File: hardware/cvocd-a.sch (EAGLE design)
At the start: 71 parts, among them IC1 PIC16F1825SO14, IC2 74HC595D, IC3 74HC595D, IC4 MCP4728_QUAD_DAC, IC5 LM324D, IC6 REG1117, IC7 6N138

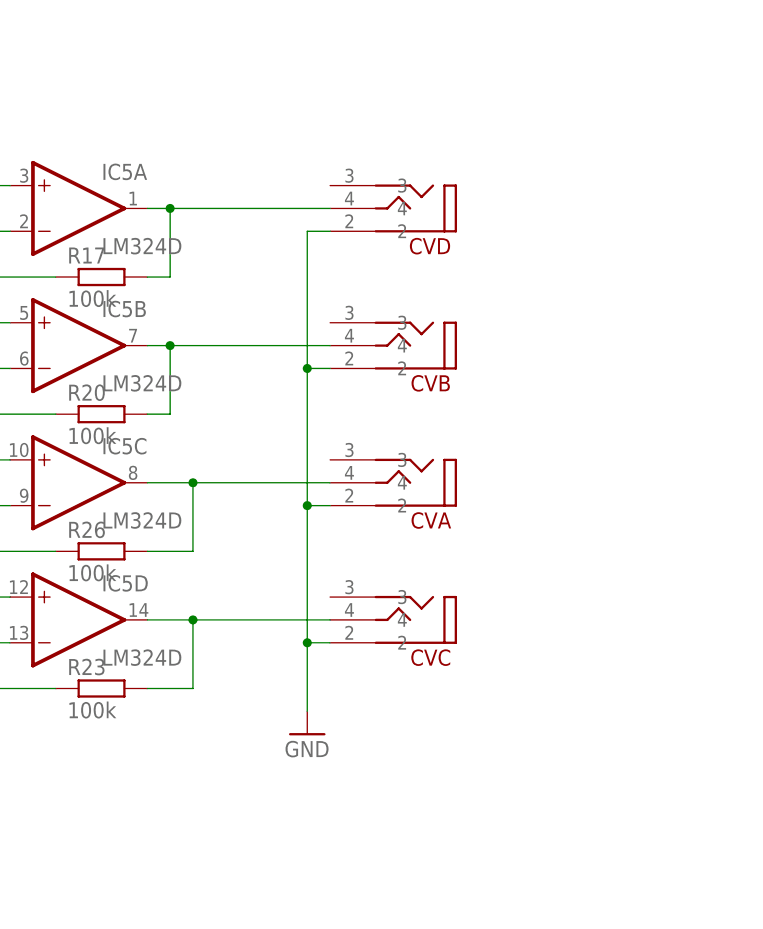
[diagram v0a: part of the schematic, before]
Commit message: icsp to top layer, current lim resistors
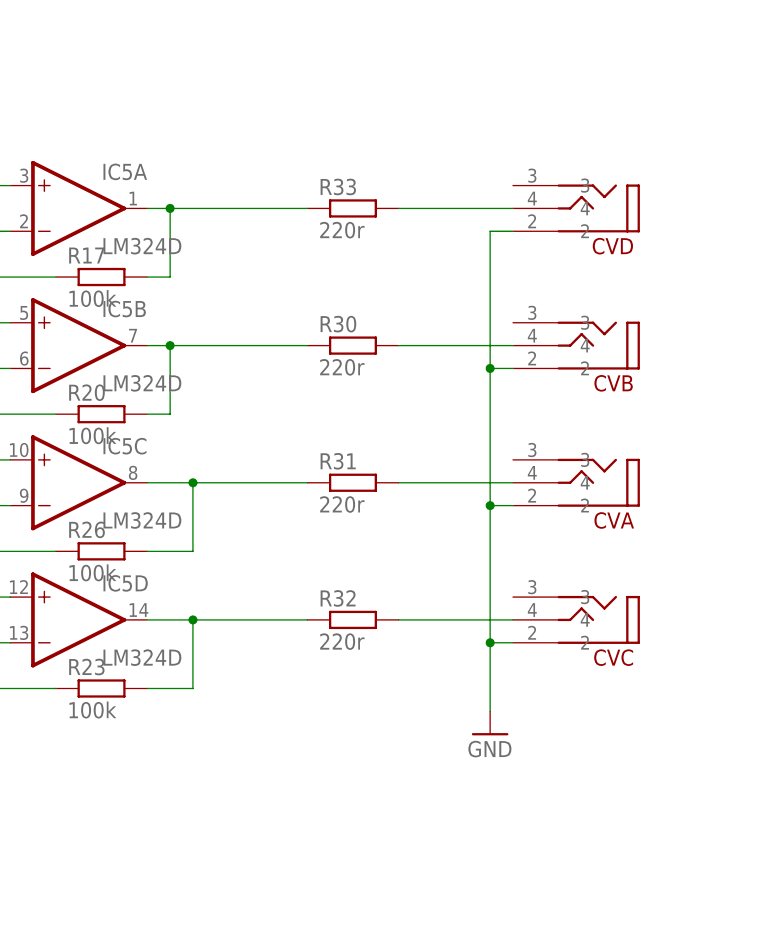
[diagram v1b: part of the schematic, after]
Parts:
- added R30, R31, R32, R33: 220r, rcl:R-EU_R0805
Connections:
- new net N$10: CVD.4, R33.2
- new net N$11: CVB.4, R30.2
- new net N$14: CVA.4, R31.2
- new net N$17: CVC.4, R32.2
- net N$2: now also R33.1; no longer CVD.4
- net N$3: now also R30.1; no longer CVB.4
- net N$4: now also R31.1; no longer CVA.4
- net N$5: now also R32.1; no longer CVC.4
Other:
- moved on the sheet: CVA, CVB, CVC, CVD
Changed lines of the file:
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@@
 <part name="C20" library="rcl" deviceset="CPOL-EU" device="C"/>
 <part name="D2" library="diode" deviceset="DIODE-" device="SOD123"/>
+<part name="R33" library="rcl" deviceset="R-EU_" device="R0805" value="220r"/>
+<part name="R30" library="rcl" deviceset="R-EU_" device="R0805" value="220r"/>
+<part name="R31" library="rcl" deviceset="R-EU_" device="R0805" value="220r"/>
+<part name="R32" library="rcl" deviceset="R-EU_" device="R0805" value="220r"/>
 </parts>
 <sheets>
@@
 </plain>
 <instances>
-<instance part="CVB" gate="G$1" x="152.4" y="99.06" rot="R180"/>
-<instance part="CVD" gate="G$1" x="152.4" y="114.3" rot="R180"/>
-<instance part="CVA" gate="G$1" x="152.4" y="83.82" rot="R180"/>
-<instance part="CVC" gate="G$1" x="152.4" y="68.58" rot="R180"/>
+<instance part="CVB" gate="G$1" x="172.72" y="99.06" rot="R180"/>
+<instance part="CVD" gate="G$1" x="172.72" y="114.3" rot="R180"/>
+<instance part="CVA" gate="G$1" x="172.72" y="83.82" rot="R180"/>
+<instance part="CVC" gate="G$1" x="172.72" y="68.58" rot="R180"/>
 <instance part="GATE4" gate="G$1" x="-15.24" y="17.78" smashed="yes" rot="R180">
 <attribute name="NAME" x="-1.778" y="17.018" size="1.778" layer="94" rot="R180"/>
@@
 <instance part="R24" gate="G$1" x="96.52" y="60.96"/>
 <instance part="GND1" gate="1" x="88.9" y="55.88"/>
-<instance part="GND13" gate="1" x="139.7" y="55.88"/>
+<instance part="GND13" gate="1" x="160.02" y="55.88"/>
 <instance part="IC3" gate="P" x="-134.62" y="-17.78" rot="R270"/>
 <instance part="GND14" gate="1" x="-149.86" y="-30.48"/>
@@
 <instance part="C20" gate="G$1" x="-55.88" y="167.64"/>
 <instance part="D2" gate="G$1" x="-106.68" y="175.26"/>
+<instance part="R33" gate="G$1" x="144.78" y="114.3"/>
+<instance part="R30" gate="G$1" x="144.78" y="99.06"/>
+<instance part="R31" gate="G$1" x="144.78" y="83.82"/>
+<instance part="R32" gate="G$1" x="144.78" y="68.58"/>
 </instances>
 <busses>
@@
 </segment>
 <segment>
-<wire x1="139.7" y1="111.76" x2="139.7" y2="96.52" width="0.1524" layer="91"/>
-<wire x1="139.7" y1="96.52" x2="139.7" y2="81.28" width="0.1524" layer="91"/>
-<wire x1="139.7" y1="81.28" x2="139.7" y2="66.04" width="0.1524" layer="91"/>
-<wire x1="139.7" y1="66.04" x2="139.7" y2="58.42" width="0.1524" layer="91"/>
+<wire x1="160.02" y1="111.76" x2="160.02" y2="96.52" width="0.1524" layer="91"/>
+<wire x1="160.02" y1="96.52" x2="160.02" y2="81.28" width="0.1524" layer="91"/>
+<wire x1="160.02" y1="81.28" x2="160.02" y2="66.04" width="0.1524" layer="91"/>
+<wire x1="160.02" y1="66.04" x2="160.02" y2="58.42" width="0.1524" layer="91"/>
 <pinref part="CVA" gate="G$1" pin="2"/>
-<wire x1="142.24" y1="81.28" x2="139.7" y2="81.28" width="0.1524" layer="91"/>
-<junction x="139.7" y="81.28"/>
+<wire x1="162.56" y1="81.28" x2="160.02" y2="81.28" width="0.1524" layer="91"/>
+<junction x="160.02" y="81.28"/>
 <pinref part="CVC" gate="G$1" pin="2"/>
-<wire x1="142.24" y1="66.04" x2="139.7" y2="66.04" width="0.1524" layer="91"/>
-<junction x="139.7" y="66.04"/>
+<wire x1="162.56" y1="66.04" x2="160.02" y2="66.04" width="0.1524" layer="91"/>
+<junction x="160.02" y="66.04"/>
 <pinref part="GND13" gate="1" pin="GND"/>
 <pinref part="CVD" gate="G$1" pin="2"/>
-<wire x1="139.7" y1="111.76" x2="142.24" y2="111.76" width="0.1524" layer="91"/>
+<wire x1="160.02" y1="111.76" x2="162.56" y2="111.76" width="0.1524" layer="91"/>
 <pinref part="CVB" gate="G$1" pin="2"/>
-<wire x1="142.24" y1="96.52" x2="139.7" y2="96.52" width="0.1524" layer="91"/>
-<junction x="139.7" y="96.52"/>
+<wire x1="162.56" y1="96.52" x2="160.02" y2="96.52" width="0.1524" layer="91"/>
+<junction x="160.02" y="96.52"/>
 </segment>
 <segment>
@@
 <wire x1="124.46" y1="106.68" x2="124.46" y2="114.3" width="0.1524" layer="91"/>
 <junction x="124.46" y="114.3"/>
-<pinref part="CVD" gate="G$1" pin="4"/>
-<wire x1="124.46" y1="114.3" x2="142.24" y2="114.3" width="0.1524" layer="91"/>
+<wire x1="124.46" y1="114.3" x2="139.7" y2="114.3" width="0.1524" layer="91"/>
+<pinref part="R33" gate="G$1" pin="1"/>
 </segment>
 </net>
@@
 <wire x1="124.46" y1="91.44" x2="124.46" y2="99.06" width="0.1524" layer="91"/>
 <junction x="124.46" y="99.06"/>
-<pinref part="CVB" gate="G$1" pin="4"/>
-<wire x1="124.46" y1="99.06" x2="142.24" y2="99.06" width="0.1524" layer="91"/>
+<wire x1="124.46" y1="99.06" x2="139.7" y2="99.06" width="0.1524" layer="91"/>
+<pinref part="R30" gate="G$1" pin="1"/>
 </segment>
 </net>
@@
 <wire x1="121.92" y1="76.2" x2="127" y2="76.2" width="0.1524" layer="91"/>
 <wire x1="127" y1="76.2" x2="127" y2="83.82" width="0.1524" layer="91"/>
-<pinref part="CVA" gate="G$1" pin="4"/>
-<wire x1="127" y1="83.82" x2="142.24" y2="83.82" width="0.1524" layer="91"/>
+<wire x1="127" y1="83.82" x2="139.7" y2="83.82" width="0.1524" layer="91"/>
 <junction x="127" y="83.82"/>
+<pinref part="R31" gate="G$1" pin="1"/>
 </segment>
 </net>
@@
 <wire x1="121.92" y1="60.96" x2="127" y2="60.96" width="0.1524" layer="91"/>
 <wire x1="127" y1="60.96" x2="127" y2="68.58" width="0.1524" layer="91"/>
-<pinref part="CVC" gate="G$1" pin="4"/>
-<wire x1="127" y1="68.58" x2="142.24" y2="68.58" width="0.1524" layer="91"/>
+<wire x1="127" y1="68.58" x2="139.7" y2="68.58" width="0.1524" layer="91"/>
 <junction x="127" y="68.58"/>
+<pinref part="R32" gate="G$1" pin="1"/>
 </segment>
 </net>
@@
 </segment>
 </net>
+<net name="N$10" class="0">
+<segment>
+<pinref part="R33" gate="G$1" pin="2"/>
+<pinref part="CVD" gate="G$1" pin="4"/>
+<wire x1="149.86" y1="114.3" x2="162.56" y2="114.3" width="0.1524" layer="91"/>
+</segment>
+</net>
+<net name="N$11" class="0">
+<segment>
+<pinref part="R30" gate="G$1" pin="2"/>
+<pinref part="CVB" gate="G$1" pin="4"/>
+<wire x1="149.86" y1="99.06" x2="162.56" y2="99.06" width="0.1524" layer="91"/>
+</segment>
+</net>
+<net name="N$14" class="0">
+<segment>
+<pinref part="R31" gate="G$1" pin="2"/>
+<pinref part="CVA" gate="G$1" pin="4"/>
+<wire x1="149.86" y1="83.82" x2="162.56" y2="83.82" width="0.1524" layer="91"/>
+</segment>
+</net>
+<net name="N$17" class="0">
+<segment>
+<pinref part="R32" gate="G$1" pin="2"/>
+<pinref part="CVC" gate="G$1" pin="4"/>
+<wire x1="149.86" y1="68.58" x2="162.56" y2="68.58" width="0.1524" layer="91"/>
+</segment>
+</net>

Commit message: working on v4
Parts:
- removed C18: 100n, rcl:C-EUC0805
- added PA, PB, PC, PD: (no value), rcl:R-TRIMM3314G
- IC1: value PIC16F1825SO14 -> 6N138; device jasons_stuff:PIC16F1825SO14 -> optocoupler:6N138
- IC2: value 74HC595D -> LM324D; device 74xx-eu:74HC595D -> linear:LM324D
- IC3: value 74HC595D -> MCP4728_QUAD_DAC; device 74xx-eu:74HC595D -> jason_eagle6:MCP4728_QUAD_DAC
- IC4: value MCP4728_QUAD_DAC -> REG1117; device jason_eagle6:MCP4728_QUAD_DAC -> burr-brown:REG1117
- IC5: value LM324D -> PIC16F1825SO14; device linear:LM324D -> jasons_stuff:PIC16F1825SO14
- IC6: value REG1117 -> 74HC595D; device burr-brown:REG1117 -> 74xx-eu:74HC595D
- IC7: value 6N138 -> 74HC595D; device optocoupler:6N138 -> 74xx-eu:74HC595D
- R10, R11, R8, R9: value (none) -> 220r
- R12, R13, R14, R15, R5, R6, R7: value (none) -> 100k
- R17, R18, R19, R23, R24, R25, R26: value 100k -> (none)
- R2, R3: value (none) -> 1k5
- R20: value 100k -> 4k7
- R22: value 4k7 -> 10k
- R27, R28: value 1k5 -> (none)
- R30, R31, R32, R33: value 220r -> (none)
- R4: value 10k -> 100k
- renumbered C10 to C5, C11 to C6, C12 to C8, C13 to C7, C19 to C1, C20 to C2, C21 to C3, C9 to C4, L1 to LED1, L2 to LED2, L3 to LED3, S1 to SW1
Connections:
- new net N$18: CVD.4, R5.2, R8.2
- new net N$19: CVB.4, R7.2, R9.2
- new net N$38: CVA.4, R11.2, R14.2
- new net N$44: CVC.4, R10.2, R12.2
- new net N$45: PA.E, R15.2
- new net N$54: PA.A, R14.1
- new net N$55: PC.E, R13.2
- new net N$56: PC.A, R12.1
- net ACT_LED: now also IC5.RA2/INT; no longer IC1.RA2/INT
- net GND: now also IC1.GND, IC2P.V-, IC3.LDAC#, IC3.VSS, IC4.GND, IC5.VSS, IC6A.G, IC6P.GND, IC7A.G, IC7P.GND, R13.1, R15.1, R23.2, R24.2, R25.2, R4.1, R6.1; no longer C18.2, IC1.VSS, IC2A.G, IC2P.GND, IC3A.G, IC3P.GND, IC4.LDAC#, IC4.VSS, IC5P.V-, IC6.GND, IC7.GND, R1.2, R18.1, R19.1, R2.2, R24.1, R25.1, R28.2
- net MIDI_IN: now also IC1.VO, IC5.RC5/RX, R2.1; no longer IC1.RC5/RX, IC7.VO, R27.1
- net MIDI_OUT: now also IC5.RC4/TX; no longer IC1.RC4/TX
- net N$1: now also R19.2; no longer R15.2
- net N$10: now also IC2A.-IN, PD.S; no longer CVD.4, R33.2
- net N$11: now also IC2C.-IN, PA.S; no longer CVB.4, R30.2
- net N$12: now also IC6A.QA, R19.1; no longer IC3A.QA, R15.1
- net N$13: now also IC6A.QB, R18.1; no longer IC3A.QB, R16.1
- net N$14: now also IC2D.-IN, PC.S; no longer CVA.4, R31.2
- net N$15: now also IC6A.QD, R17.1; no longer IC3A.QD, R13.1
- net N$16: now also IC6A.QC, R16.1; no longer IC3A.QC, R14.1
- net N$17: now also PD.E, R4.2; no longer CVC.4, R32.2
- net N$2: now also IC2A.OUT, R8.1; no longer IC5A.OUT, R17.2, R33.1
- net N$20: now also R26.2; no longer R8.2
- net N$21: now also IC3.SCL, IC5.RCO/SCL/SCK, R21.2; no longer IC1.RCO/SCL/SCK, IC4.SCL, R22.2
- net N$22: now also IC3.SDA, IC5.RC1/SDA/SDI, R20.2; no longer IC1.RC1/SDA/SDI, IC4.SDA, R21.2
- net N$23: now also R27.2; no longer R7.2
- net N$24: now also R28.2; no longer R6.2
- net N$25: now also PD.A, R5.1; no longer IC5A.-IN, R17.1, R18.2
- net N$26: now also IC2B.-IN, PB.S; no longer IC5B.-IN, R19.2, R20.1
- net N$27: now also PB.E, R6.2; no longer IC5C.-IN, R25.2, R26.1
- net N$28: now also PB.A, R7.1; no longer IC5D.-IN, R23.1, R24.2
- net N$29: now also R1.1; no longer R29.1
- net N$3: now also IC2B.OUT, R9.1; no longer IC5B.OUT, R20.2, R30.1
- net N$30: now also IC1.A, R1.2; no longer IC7.A, R29.2
- net N$31: now also IC1.C; no longer IC7.C
- net N$32: now also R29.2; no longer R5.2
- net N$33: now also R30.2; no longer R12.2
- net N$34: now also IC5.RA3/MCLR#/VPP; no longer IC1.RA3/MCLR#/VPP
- net N$35: now also R25.1; no longer R1.1
- net N$36: now also R23.1; no longer R3.1
- net N$37: now also R24.1; no longer R2.1
- net N$39: now also R31.2; no longer R11.2
- net N$4: now also IC2C.OUT, R11.1; no longer IC5C.OUT, R26.2, R31.1
- net N$41: now also R32.2; no longer R10.2
- net N$42: now also IC1.VB, R3.1; no longer IC7.VB, R28.1
- net N$43: now also IC7A.QA, R26.1; no longer IC2A.QA, R8.1
- net N$46: now also IC7A.QB, R27.1; no longer IC2A.QB, R7.1
- net N$47: now also IC7A.QD, R29.1; no longer IC2A.QD, R5.1
- net N$48: now also IC7A.QC, R28.1; no longer IC2A.QC, R6.1
- net N$49: now also IC7A.QF, R31.1; no longer IC2A.QF, R11.1
- net N$5: now also IC2D.OUT, R10.1; no longer IC5D.OUT, R23.2, R32.1
- net N$50: now also IC7A.QG, R32.1; no longer IC2A.QG, R10.1
- net N$51: now also IC7A.QE, R30.1; no longer IC2A.QE, R12.1
- net N$52: now also R33.2; no longer R9.2
- net N$53: now also IC7A.QH, R33.1; no longer IC2A.QH, R9.1
- net N$6: now also R18.2; no longer R16.2
- net N$7: now also R16.2; no longer R14.2
- net N$8: now also R17.2; no longer R13.2
- net N$9: now also IC5.RC3/SS#, R22.2; no longer IC1.RC3/SS#, R4.2
- net SR_CLK: now also IC5.RA4/SDO, IC6A.SCK, IC7A.SCK; no longer IC1.RA4/SDO, IC2A.SCK, IC3A.SCK
- net SR_DAT: now also IC5.RA0/ICSPDAT, IC6A.SER; no longer IC1.RA0/ICSPDAT, IC3A.SER
- net SR_DAT2: now also IC5.RA1/ICPCLK, IC7A.SER; no longer IC1.RA1/ICPCLK, IC2A.SER
- net SR_RCK: now also IC5.RA5, IC6A.RCK, IC7A.RCK; no longer IC1.RA5, IC2A.RCK, IC3A.RCK
- net STATUS_LED: now also IC5.RC2; no longer IC1.RC2
- net VDD: now also IC1.VCC, IC3.VDD, IC4.VOUT, IC5.VDD, IC6A.SCL, IC6P.VCC, IC7A.SCL, IC7P.VCC, R2.2, R20.1; no longer IC1.VDD, IC2A.SCL, IC2P.VCC, IC3A.SCL, IC3P.VCC, IC4.VDD, IC6.VOUT, IC7.VCC, R27.2, R4.1
- net VIN: now also IC2P.V+, IC4.VIN; no longer C18.1, IC5P.V+, IC6.VIN
- net VOUTA: now also IC2B.+IN, IC3.VOUTA; no longer IC4.VOUTA, IC5B.+IN
- net VOUTB: now also IC2A.+IN, IC3.VOUTB; no longer IC4.VOUTB, IC5A.+IN
- net VOUTC: now also IC2D.+IN, IC3.VOUTC; no longer IC4.VOUTC, IC5D.+IN
- net VOUTD: now also IC2C.+IN, IC3.VOUTD; no longer IC4.VOUTD, IC5C.+IN
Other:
- moved on the sheet: R1, R10, R11, R12, R13, R14, R15, R16, R17, R18, R19, R2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

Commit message: REV4 RELEASE CANDIDATE
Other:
- note added: "12 BIT DAC"
- note added: "CV 2 X GAIN OUTPUT BUFFER"
- note added: "CV.OCD MIDI TO CV CONVERTER"
- note added: "GATES 1-4"
- note added: "GATES 5-12"
- note added: "INDICATORS"
- note added: "Jason Hotchkiss, Sixty-Four Pixels Ltd"
- note added: "MIDI IN"
- note added: "POWER SUPPLY"
- note added: "PROCESSOR"
- note added: "REVISION 4, 30 JAN 2018"
- moved on the sheet: LED1, LED2, LED3, R23, R24, R25
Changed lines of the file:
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@@
 <sheet>
 <plain>
+<text x="59.436" y="172.212" size="3.81" layer="95">CV.OCD MIDI TO CV CONVERTER</text>
+<text x="59.944" y="166.37" size="3.81" layer="95">REVISION 4, 30 JAN 2018</text>
+<text x="59.944" y="160.782" size="3.81" layer="95">Jason Hotchkiss, Sixty-Four Pixels Ltd</text>
+<text x="-152.4" y="185.42" size="3.81" layer="95">POWER SUPPLY</text>
+<text x="-152.4" y="154.94" size="3.81" layer="95">MIDI IN</text>
+<text x="-86.868" y="65.024" size="3.81" layer="95">PROCESSOR</text>
+<text x="16.256" y="62.738" size="3.81" layer="95">12 BIT DAC</text>
+<text x="93.726" y="123.444" size="3.81" layer="95">CV 2 X GAIN OUTPUT BUFFER</text>
+<text x="-91.694" y="-16.256" size="3.81" layer="95">GATES 1-4</text>
+<text x="103.886" y="-36.576" size="3.81" layer="95">GATES 5-12</text>
+<text x="-1.778" y="120.142" size="3.81" layer="95">INDICATORS</text>
+<wire x1="58.42" y1="177.8" x2="58.42" y2="158.496" width="0.1524" layer="95"/>
+<wire x1="58.42" y1="158.496" x2="154.94" y2="158.496" width="0.1524" layer="95"/>
+<wire x1="154.94" y1="158.496" x2="154.94" y2="177.8" width="0.1524" layer="95"/>
+<wire x1="154.94" y1="177.8" x2="58.42" y2="177.8" width="0.1524" layer="95"/>
 </plain>
 <instances>
@@
 <instance part="GND18" gate="1" x="-93.98" y="33.02"/>
 <instance part="GND19" gate="1" x="7.62" y="58.42"/>
-<instance part="LED3" gate="G$1" x="5.08" y="182.88"/>
-<instance part="LED1" gate="G$1" x="12.7" y="182.88"/>
-<instance part="R25" gate="G$1" x="5.08" y="170.18" rot="R270"/>
-<instance part="R23" gate="G$1" x="12.7" y="170.18" rot="R270"/>
-<instance part="R24" gate="G$1" x="20.32" y="170.18" rot="R270"/>
-<instance part="LED2" gate="G$1" x="20.32" y="182.88"/>
-<instance part="GND21" gate="1" x="5.08" y="160.02"/>
-<instance part="GND22" gate="1" x="12.7" y="160.02"/>
-<instance part="GND23" gate="1" x="20.32" y="160.02"/>
+<instance part="LED3" gate="G$1" x="5.08" y="152.4"/>
+<instance part="LED1" gate="G$1" x="12.7" y="152.4"/>
+<instance part="R25" gate="G$1" x="5.08" y="139.7" rot="R270"/>
+<instance part="R23" gate="G$1" x="12.7" y="139.7" rot="R270"/>
+<instance part="R24" gate="G$1" x="20.32" y="139.7" rot="R270"/>
+<instance part="LED2" gate="G$1" x="20.32" y="152.4"/>
+<instance part="GND21" gate="1" x="5.08" y="129.54"/>
+<instance part="GND22" gate="1" x="12.7" y="129.54"/>
+<instance part="GND23" gate="1" x="20.32" y="129.54"/>
 <instance part="IC4" gate="G$1" x="-76.2" y="175.26"/>
 <instance part="GND4" gate="1" x="-76.2" y="154.94"/>
@@
 <pinref part="GND21" gate="1" pin="GND"/>
 <pinref part="R25" gate="G$1" pin="2"/>
-<wire x1="5.08" y1="162.56" x2="5.08" y2="165.1" width="0.1524" layer="91"/>
+<wire x1="5.08" y1="132.08" x2="5.08" y2="134.62" width="0.1524" layer="91"/>
 </segment>
 <segment>
 <pinref part="GND22" gate="1" pin="GND"/>
 <pinref part="R23" gate="G$1" pin="2"/>
-<wire x1="12.7" y1="162.56" x2="12.7" y2="165.1" width="0.1524" layer="91"/>
+<wire x1="12.7" y1="132.08" x2="12.7" y2="134.62" width="0.1524" layer="91"/>
 </segment>
 <segment>
 <pinref part="GND23" gate="1" pin="GND"/>
 <pinref part="R24" gate="G$1" pin="2"/>
-<wire x1="20.32" y1="162.56" x2="20.32" y2="165.1" width="0.1524" layer="91"/>
+<wire x1="20.32" y1="132.08" x2="20.32" y2="134.62" width="0.1524" layer="91"/>
 </segment>
 <segment>
@@
 <pinref part="R25" gate="G$1" pin="1"/>
 <pinref part="LED3" gate="G$1" pin="C"/>
-<wire x1="5.08" y1="175.26" x2="5.08" y2="177.8" width="0.1524" layer="91"/>
+<wire x1="5.08" y1="144.78" x2="5.08" y2="147.32" width="0.1524" layer="91"/>
 </segment>
 </net>
@@
 <pinref part="R23" gate="G$1" pin="1"/>
 <pinref part="LED1" gate="G$1" pin="C"/>
-<wire x1="12.7" y1="175.26" x2="12.7" y2="177.8" width="0.1524" layer="91"/>
+<wire x1="12.7" y1="144.78" x2="12.7" y2="147.32" width="0.1524" layer="91"/>
 </segment>
 </net>
@@
 <pinref part="R24" gate="G$1" pin="1"/>
 <pinref part="LED2" gate="G$1" pin="C"/>
-<wire x1="20.32" y1="175.26" x2="20.32" y2="177.8" width="0.1524" layer="91"/>
+<wire x1="20.32" y1="144.78" x2="20.32" y2="147.32" width="0.1524" layer="91"/>
 </segment>
 </net>
@@
 <segment>
 <pinref part="LED1" gate="G$1" pin="A"/>
-<wire x1="12.7" y1="185.42" x2="12.7" y2="193.04" width="0.1524" layer="91"/>
-<label x="12.7" y="190.5" size="1.778" layer="95" rot="R90"/>
+<wire x1="12.7" y1="154.94" x2="12.7" y2="162.56" width="0.1524" layer="91"/>
+<label x="12.7" y="160.02" size="1.778" layer="95" rot="R90"/>
 </segment>
 <segment>
@@
 <segment>
 <pinref part="LED2" gate="G$1" pin="A"/>
-<wire x1="20.32" y1="185.42" x2="20.32" y2="193.04" width="0.1524" layer="91"/>
-<label x="20.32" y="190.5" size="1.778" layer="95" rot="R90"/>
+<wire x1="20.32" y1="154.94" x2="20.32" y2="162.56" width="0.1524" layer="91"/>
+<label x="20.32" y="160.02" size="1.778" layer="95" rot="R90"/>
 </segment>
 <segment>
@@
 <segment>
 <pinref part="LED3" gate="G$1" pin="A"/>
-<wire x1="5.08" y1="185.42" x2="5.08" y2="193.04" width="0.1524" layer="91"/>
-<label x="2.54" y="193.04" size="1.778" layer="95"/>
-</segment>
-<segment>
+<wire x1="5.08" y1="154.94" x2="5.08" y2="162.56" width="0.1524" layer="91"/>
+<label x="2.54" y="162.56" size="1.778" layer="95"/>
+</segment>
+<segment>

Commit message: v5 board first version
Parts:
- removed PA, PB, PC, PD: (no value), rcl:R-TRIMM3314G
- added C10, C11, C12, C9: 22p, rcl:C-EUC0805
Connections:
- removed net N$17: PD.E, R4.2
- removed net N$25: PD.A, R5.1
- removed net N$27: PB.E, R6.2
- removed net N$28: PB.A, R7.1
- removed net N$45: PA.E, R15.2
- removed net N$54: PA.A, R14.1
- removed net N$55: PC.E, R13.2
- removed net N$56: PC.A, R12.1
- net N$10: now also C9.2, R4.2, R5.1; no longer PD.S
- net N$11: now also C11.2, R14.1, R15.2; no longer PA.S
- net N$14: now also C12.2, R12.1, R13.2; no longer PC.S
- net N$2: now also C9.1
- net N$26: now also C10.2, R6.2, R7.1; no longer PB.S
- net N$3: now also C10.1
- net N$4: now also C11.1
- net N$5: now also C12.1
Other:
- moved on the sheet: CVA, CVB, CVC, CVD, R10, R11, R12, R14, R5, R7, R8, R9
